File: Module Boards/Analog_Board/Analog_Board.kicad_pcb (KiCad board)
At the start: 2 copper layers, 35 parts, among them J1 212134-0003, J2 212134-0003, J3 212134-0003, J4 212134-0003, U1 LTC1864LIMS8#PBF, U2 TXB0104RUTR, U3 TPS22916CYFPR, U4 TPS7A9401DSCR, U5 TMUX1104DQAR

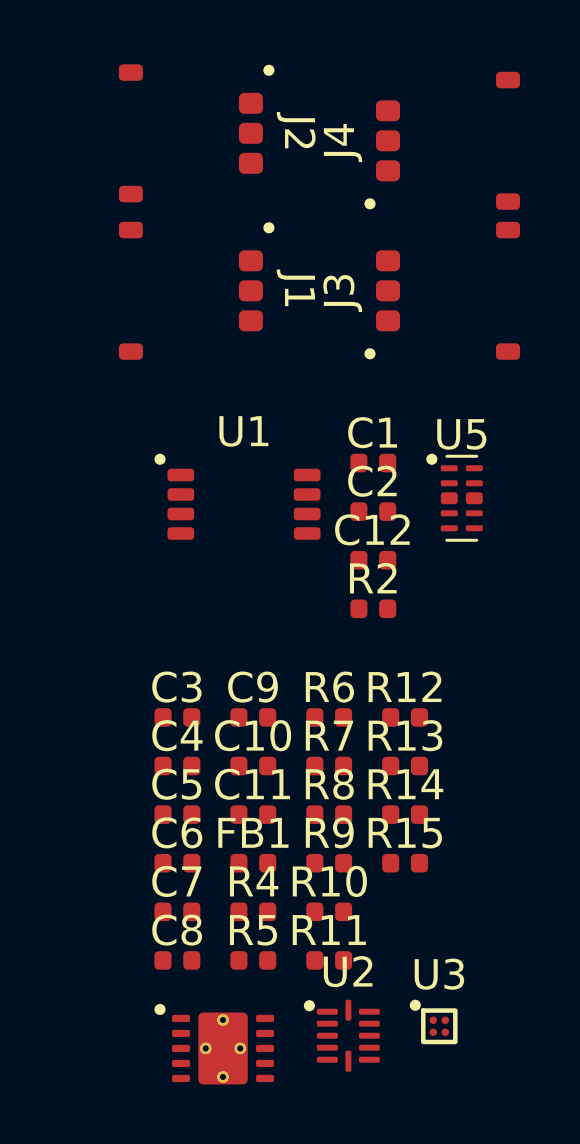
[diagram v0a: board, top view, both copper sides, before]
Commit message: Routed Analog Board
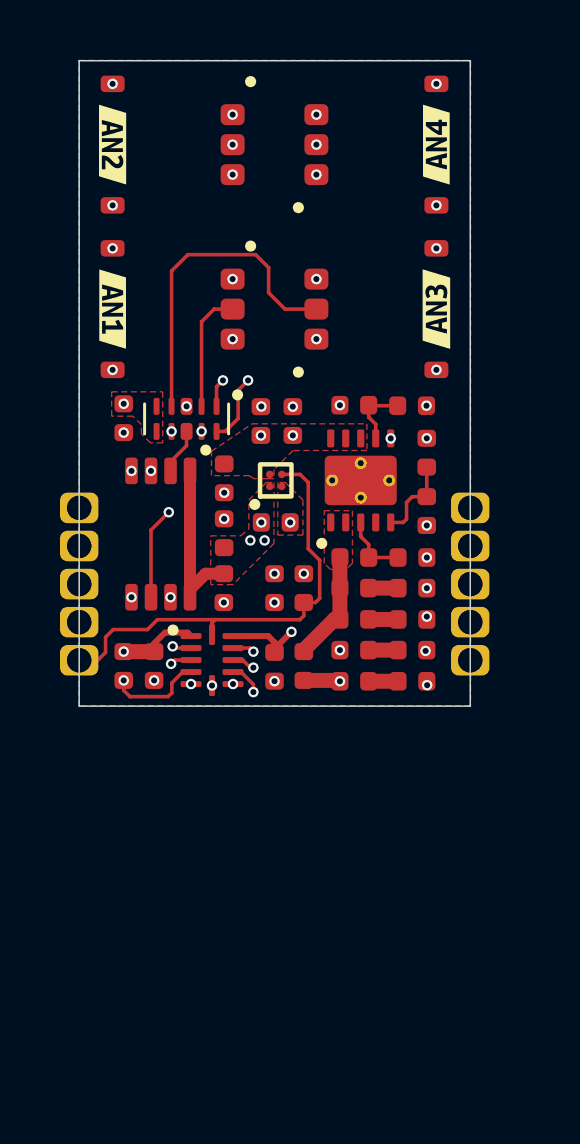
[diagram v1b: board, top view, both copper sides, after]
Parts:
- added C13: 100n 10V, X-MODs_PcbLib:C0402, F.Cu at (135.5, 83.2)
- added G***: LOGO, LOGO, B.Cu at (135.5, 70.4)
- added G***: LOGO, LOGO, B.Cu at (135.8, 83.8)
- added J5: ~, X-MODs_PcbLib:Analog_Board_Castellated_Conn_1.27mm, F.Cu at (135.5, 78.6)
- added kibuzzard-66E06AA7: G***, kibuzzard-66E06AA7, B.Cu at (135.5, 87.9)
- added kibuzzard-66E06AC0: G***, kibuzzard-66E06AC0, B.Cu at (135.5, 77.7)
- added kibuzzard-671558EF: G***, kibuzzard-671558EF, F.Cu at (140.9, 76.1)
- added kibuzzard-6715591F: G***, kibuzzard-6715591F, F.Cu at (140.9, 70.6)
- added kibuzzard-67155927: G***, kibuzzard-67155927, F.Cu at (130.1, 70.6)
- added kibuzzard-6715592C: G***, kibuzzard-6715592C, F.Cu at (130.1, 76.1)
- added kibuzzard-671559FE: G***, kibuzzard-671559FE, B.Cu at (135.5, 73.9)
- moved U4 19.5 mm to (138.4, 81.8), turned to 90 degrees
- moved U3 19.0 mm to (135.5, 81.8), turned to 90 degrees
- moved C11 14.1 mm to (138.2, 79.3), turned to 180 degrees
- moved C8 13.7 mm to (138.2, 85.4)
- moved R14 13.6 mm to (140.1, 79.3)
- moved U2 13.3 mm to (133.4, 87.8)
- moved R11 12.7 mm to (140.1, 85.4)
- moved R8 12.5 mm to (140.6, 80.9), turned to -90 degrees
- moved C4 11.8 mm to (135.0, 79.8), turned to -90 degrees
- moved R15 11.8 mm to (140.6, 82.8), turned to -90 degrees
- moved C10 11.6 mm to (136.1, 79.8), turned to 90 degrees
- moved R4 10.9 mm to (136.5, 85.4), turned to -90 degrees
- moved R5 10.7 mm to (130.5, 88.0), turned to -90 degrees
- moved C7 9.69 mm to (138.2, 88.5)
- moved C12 9.57 mm to (130.5, 79.7), turned to -90 degrees
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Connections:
- net Net-(U1-IN+) renamed /[2] ADC & Multiplexer/ADC_IN
- net Net-(U4-FB_PG) renamed /[1] Power Regulation & Level Shifting/FB_PG
- net Net-(U5-S1) renamed /[2] ADC & Multiplexer/AN_1
- net Net-(U5-S2) renamed /[2] ADC & Multiplexer/AN_2
- net Net-(U5-S3) renamed /[2] ADC & Multiplexer/AN_3
- net Net-(U5-S4) renamed /[2] ADC & Multiplexer/AN_4
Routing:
- net +3VA_ADC: track 0.00 -> 33.8 mm, vias 0 -> 8
- net SPI_CS_3V: track 0.00 -> 19.8 mm, vias 0 -> 3
- net /[2] ADC & Multiplexer/AN_4: track 0.00 -> 16.2 mm, vias 0 -> 2
- net +3VA: track 0.00 -> 16.1 mm, vias 0 -> 4
- net +1V8: track 0.00 -> 15.4 mm, vias 0 -> 1
- net ADC_EN: track 0.00 -> 15.0 mm
- net MUX_A0: track 0.00 -> 14.6 mm, vias 0 -> 1
- net MUX_A1: track 0.00 -> 14.2 mm, vias 0 -> 1
- net /[2] ADC & Multiplexer/AN_3: track 0.00 -> 10.8 mm
- net /[2] ADC & Multiplexer/AN_2: track 0.00 -> 9.99 mm, vias 0 -> 2
- net Net-(U1-SDO): track 0.00 -> 8.06 mm, vias 0 -> 2
- net SPI_SCK_1V8: track 0.00 -> 7.61 mm, vias 0 -> 1
- net SPI_CS_1V8: track 0.00 -> 7.51 mm, vias 0 -> 1
- net +3V3: track 0.00 -> 6.74 mm, vias 0 -> 2
- net SPI_MISO_1V8: track 0.00 -> 6.64 mm, vias 0 -> 1
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- added copper zone on F.Cu, net +3VA
- added copper zone on F.Cu, net +3VA_ADC
- added copper zone on F.Cu, net /[1] Power Regulation & Level Shifting/+3V3_FILT
- added copper zone on B.Cu, net GND
- added copper zone on F.Cu, net GND
- added copper zone on In1.Cu, net GND
- added copper zone on In3.Cu, net GND
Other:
- board outline added: 13 x 21.5 mm
- copper layers 2 -> 6
